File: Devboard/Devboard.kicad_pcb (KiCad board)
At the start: 2 copper layers, 38.7 x 50.6 mm, 38 parts, among them J1 USB_C_Receptacle_USB2.0_14P, J2 Conn_01x20, J3 Conn_01x20, J4 Conn_01x03, SW1 SW_Push, SW2 SW_Push, U1 RP2040, U2 MCP1700x-120xxMB, U3 W25Q128JVS, U4 ER_OLEDM0.91_1x-I2C, Y2 Crystal_GND24

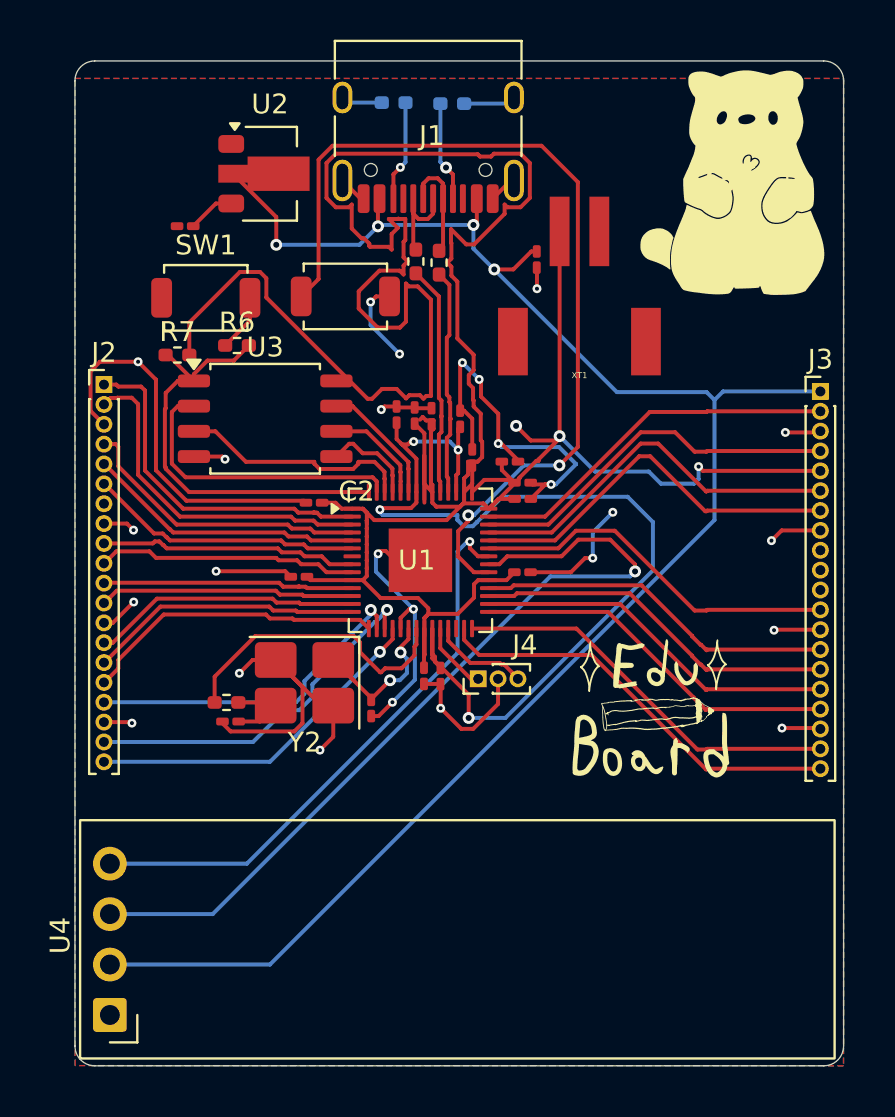
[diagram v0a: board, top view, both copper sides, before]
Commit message: Added the TPS63000 buck-boost converter
Next, I need to route everything again. I also need to finish the BOM. The silkscreen could also use some work imo. I also had to change some of the symbols. I will likely be doing pcba.

https://lapse.hackclub.com/timelapse/hDr_HyoGHTTv

https://lapse.hackclub.com/timelapse/UjBjIMcLNt3x
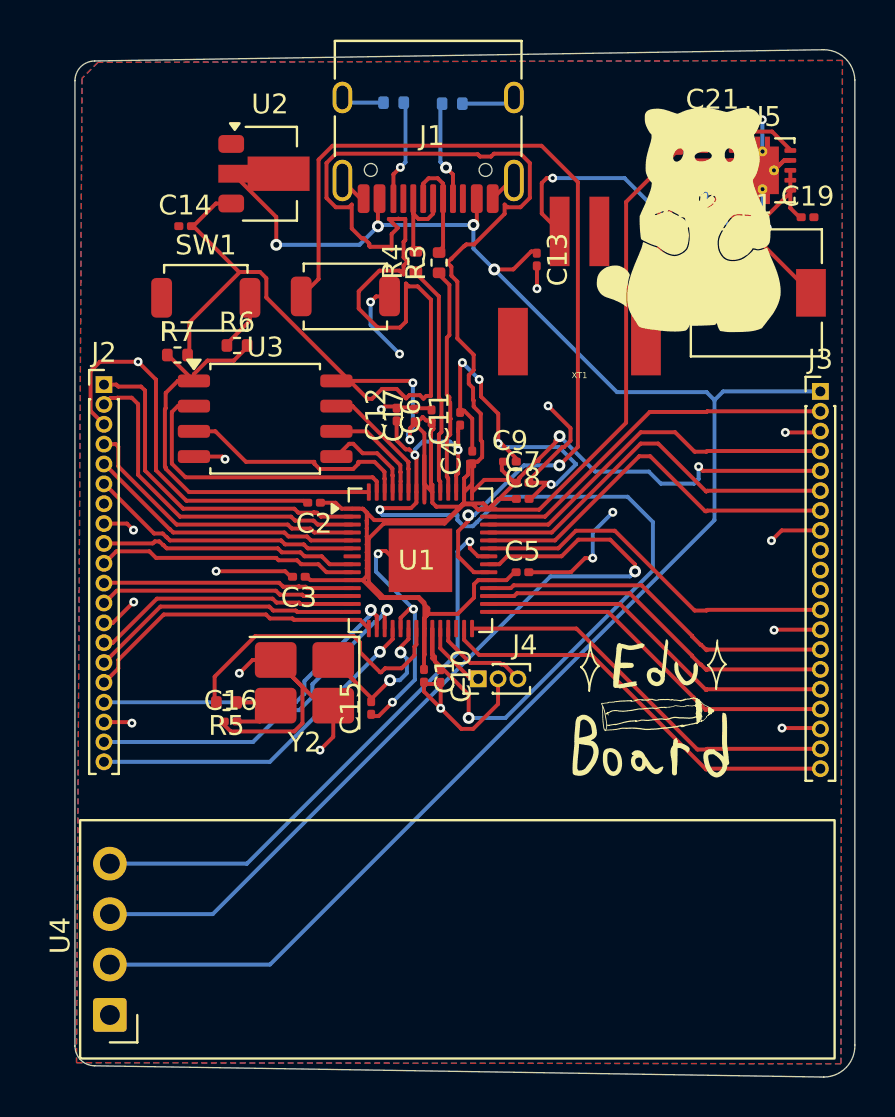
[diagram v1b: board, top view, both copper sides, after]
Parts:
- added C18: 10μf, Capacitor_SMD:C_0201_0603Metric, F.Cu at (168.2, 53.2)
- added C19: 0.1μf, Capacitor_SMD:C_0201_0603Metric, F.Cu at (174.7, 54.4)
- added C20: 10μf, Capacitor_SMD:C_0201_0603Metric, F.Cu at (168.6, 51.0)
- added C21: 10μf, Capacitor_SMD:C_0201_0603Metric, F.Cu at (169.9, 49.5)
- added L1: 2.2μH, Inductor_SMD:L_6.3x6.3_H3, F.Cu at (172.2, 58.2)
- added R8: 100Ω, Resistor_SMD:R_0201_0603Metric, F.Cu at (169.7, 54.3)
- added U5: TPS63000, Package_SON:Texas_DRC0010J_ThermalVias, F.Cu at (172.5, 52.0)
- C1, C10, C11, C12, C13, C14, C15, C16, C17, C2, C3, C4, C5, C6, C7, C8, C9: footprint Capacitor_SMD:C_0201_0603Metric_Pad0.64x0.40mm_HandSolder -> Capacitor_SMD:C_0201_0603Metric
- R1, R2, R3, R4, R5, R6, R7: footprint Resistor_SMD:R_0402_1005Metric_Pad0.72x0.64mm_HandSolder -> Resistor_SMD:R_0402_1005Metric
- moved G*** 2.89 mm to (169.7, 54.3)
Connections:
- C14 pad 2: Net-(U2-VO) -> +3V3
- U2 pad 3: Net-(U2-VO) -> +3V3
- XT1 pad 1: +3V3 -> LipoVIN
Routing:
- net +3V3: track 167.0 -> 211.3 mm, vias 3 -> 4
- net GND: track 117.9 -> 135.9 mm, vias 26 -> 31
- net LipoVIN: track 0.00 -> 15.8 mm, vias 0 -> 2
- net Net-(U5-L2): track 0.00 -> 10.5 mm
- net Net-(U5-L1): track 0.00 -> 9.59 mm, vias 0 -> 2
- net Net-(U5-EN): track 0.00 -> 7.01 mm
- net Net-(U2-VO): track 2.38 -> 0.00 mm
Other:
- board size 38.7 x 50.6 mm -> 39.3 x 51.7 mm

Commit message: Journaled and worked on getting a render done.
I got a basic render working with the silkscreen. Orignally I had trouble trying to make the silscreen show up. The solution was to raise the silkscreen above the rest of the pcb 3d model.
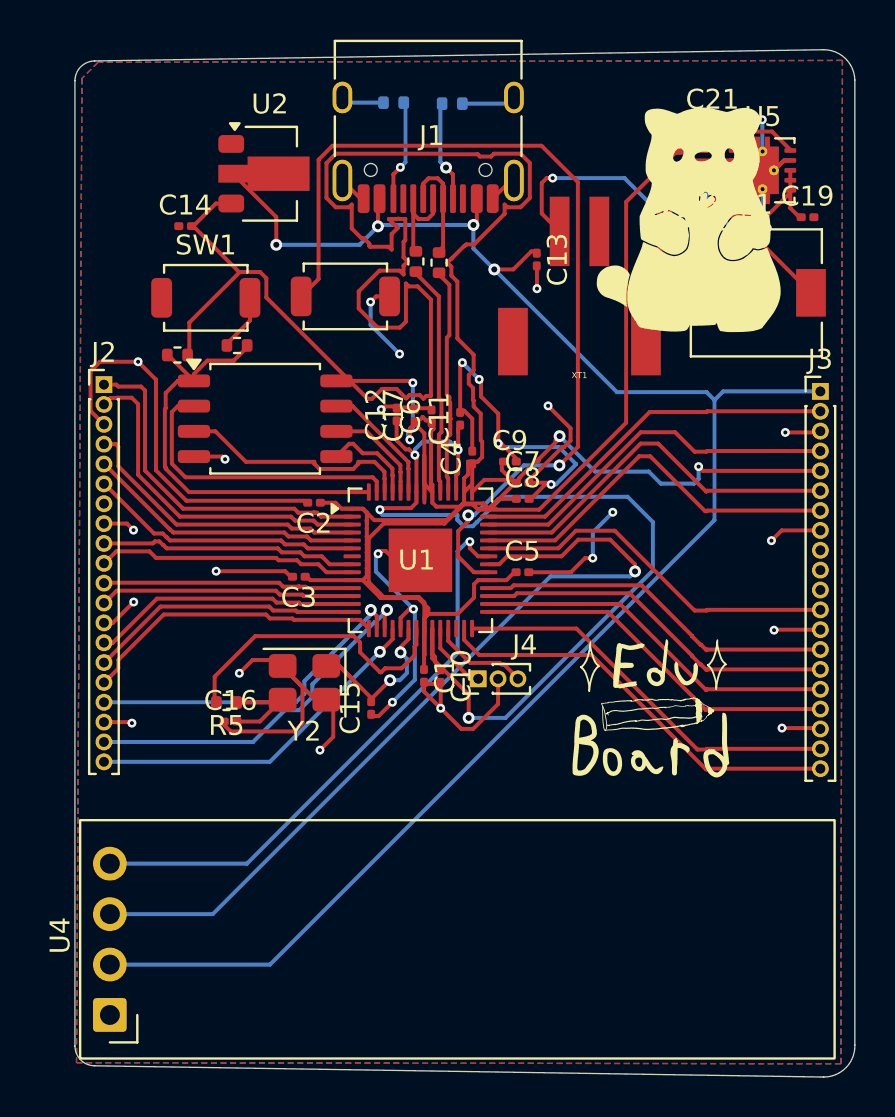
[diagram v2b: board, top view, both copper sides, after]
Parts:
- R1: value 5.1lK -> 5.1KΩ
- R2: value 5.1K -> 5.1KΩ
- R3, R4: value 27 -> 27Ω
- R6: value 1K -> 1KΩ
- R7: value 10K -> 10KΩ
- Y2: footprint Crystal:Crystal_SMD_3225-4Pin_3.2x2.5mm_HandSoldering -> Crystal:Crystal_SMD_3225-4Pin_3.2x2.5mm
